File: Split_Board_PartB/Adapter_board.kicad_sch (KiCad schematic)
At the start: 2 parts, among them J2 Conn_01x37, J6 Conn_01x30

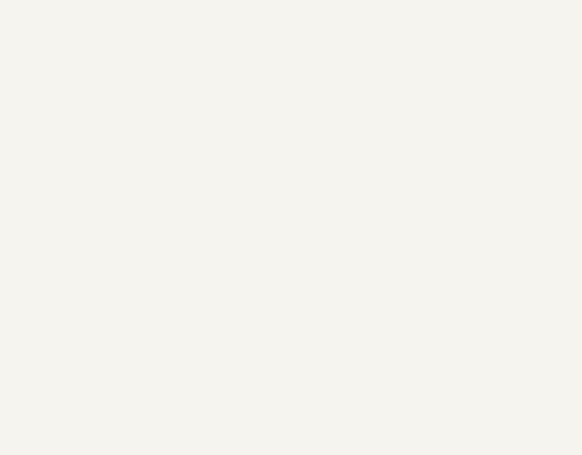
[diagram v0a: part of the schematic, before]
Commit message: added a led pins on part A connecttor, added adapter board  and led connector on adapter board, added pdf of design files of voidron part b is upto date part A final is remaining. Adapter board is also ok
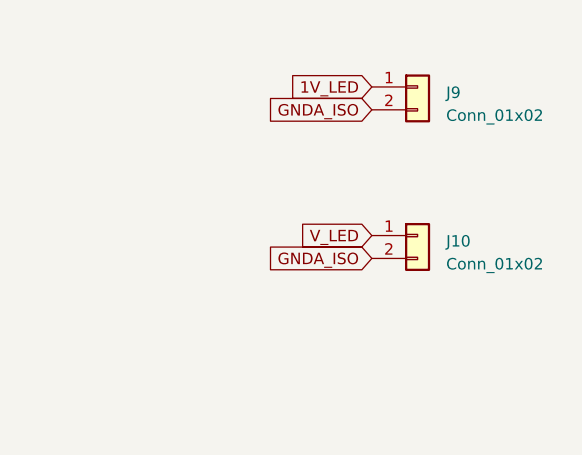
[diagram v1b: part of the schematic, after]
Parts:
- added J10, J9: Conn_01x02, symbol Connector_Generic:Conn_01x02
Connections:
- net 1V_LED: now also J9.1 (Pin_1)
- net GNDA_ISO: now also J10.2 (Pin_2), J9.2 (Pin_2)
- net V_LED: now also J10.1 (Pin_1)
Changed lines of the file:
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@@
+    )
+  )
+  (global_label "GNDA_ISO" (shape input) (at 227.965 60.325 180) (fields_autoplaced)
+    (effects (font (size 1.27 1.27)) (justify right))
+    (property "Intersheetrefs" "${INTERSHEET_REFS}" (at 215.9877 60.325 0)
+      (effects (font (size 1.27 1.27)) (justify right) hide)
     )
   )
@@
     )
   )
+  (global_label "1V_LED" (shape input) (at 227.965 57.785 180)
+    (effects (font (size 1.27 1.27)) (justify right))
+    (property "Intersheetrefs" "${INTERSHEET_REFS}" (at 227.965 57.785 0)
+      (effects (font (size 1.27 1.27)) hide)
+    )
+  )
   (global_label "CS0_ISO" (shape bidirectional) (at 120.65 88.265 0)
     (effects (font (size 1.27 1.27)) (justify left))
@@
     )
   )
+  (global_label "GNDA_ISO" (shape input) (at 227.965 76.835 180) (fields_autoplaced)
+    (effects (font (size 1.27 1.27)) (justify right))
+    (property "Intersheetrefs" "${INTERSHEET_REFS}" (at 215.9877 76.835 0)
+      (effects (font (size 1.27 1.27)) (justify right) hide)
+    )
+  )
   (global_label "1OUT_4" (shape input) (at 174.625 67.945 180)
     (effects (font (size 1.27 1.27)) (justify right))
@@
     )
   )
+  (global_label "V_LED" (shape input) (at 227.965 74.295 180)
+    (effects (font (size 1.27 1.27)) (justify right))
+    (property "Intersheetrefs" "${INTERSHEET_REFS}" (at 227.965 74.295 0)
+      (effects (font (size 1.27 1.27)) hide)
+    )
+  )
   (global_label "1OUT_1" (shape input) (at 120.65 60.325 0)
     (effects (font (size 1.27 1.27)) (justify left))
@@
     )
   )
+  (symbol (lib_id "Connector_Generic:Conn_01x02") (at 233.045 57.785 0) (unit 1)
+    (in_bom yes) (on_board yes) (dnp no) (fields_autoplaced)
+    (property "Reference" "J9" (at 236.22 58.42 0)
+      (effects (font (size 1.27 1.27)) (justify left))
+    )
+    (property "Value" "Conn_01x02" (at 236.22 60.96 0)
+      (effects (font (size 1.27 1.27)) (justify left))
+    )
+    (property "Footprint" "" (at 233.045 57.785 0)
+      (effects (font (size 1.27 1.27)) hide)
+    )
+    (property "Datasheet" "~" (at 233.045 57.785 0)
+      (effects (font (size 1.27 1.27)) hide)
+    )
+    (pin "1")
+    (pin "2")
+    (instances
+      (project "Split_Board_PartB"
+        (path "/e2d56ecd-77dd-4fed-8d81-4a7d32aa0989/7845fef2-53d4-4305-b651-11508440e42d"
+          (reference "J9") (unit 1)
+        )
+      )
+    )
+  )
+  (symbol (lib_id "Connector_Generic:Conn_01x02") (at 233.045 74.295 0) (unit 1)
+    (in_bom yes) (on_board yes) (dnp no) (fields_autoplaced)
+    (property "Reference" "J10" (at 236.22 74.93 0)
+      (effects (font (size 1.27 1.27)) (justify left))
+    )
+    (property "Value" "Conn_01x02" (at 236.22 77.47 0)
+      (effects (font (size 1.27 1.27)) (justify left))
+    )
+    (property "Footprint" "" (at 233.045 74.295 0)
+      (effects (font (size 1.27 1.27)) hide)
+    )
+    (property "Datasheet" "~" (at 233.045 74.295 0)
+      (effects (font (size 1.27 1.27)) hide)
+    )
+    (pin "1")
+    (pin "2")
+    (instances
+      (project "Split_Board_PartB"
+        (path "/e2d56ecd-77dd-4fed-8d81-4a7d32aa0989/7845fef2-53d4-4305-b651-11508440e42d"
+          (reference "J10") (unit 1)
+        )
+      )
+    )
+  )
